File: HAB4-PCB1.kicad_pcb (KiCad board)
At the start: 2 copper layers, 16 parts, among them J1 Barrel_Jack_Switch

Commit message: gnd plane
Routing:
- net Net-(D1-K): track 9.56 -> 44.2 mm, vias 0 -> 1
- net GND: vias 0 -> 12
- added copper zone on B.Cu, net GND
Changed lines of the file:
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@@
 		)
+	)
+	(via
+		(at 23.99 66)
+		(size 0.6)
+		(drill 0.3)
+		(layers "F.Cu" "B.Cu")
+		(net 1)
+	)
+	(via
+		(at 21 19.5)
+		(size 0.6)
+		(drill 0.3)
+		(layers "F.Cu" "B.Cu")
+		(net 1)
+	)
+	(via
+		(at 104 89.54)
+		(size 0.6)
+		(drill 0.3)
+		(layers "F.Cu" "B.Cu")
+		(net 1)
+	)
+	(via
+		(at 59.62 15.92)
+		(size 0.6)
+		(drill 0.3)
+		(layers "F.Cu" "B.Cu")
+		(net 1)
+	)
+	(via
+		(at 44.38 15.92)
+		(size 0.6)
+		(drill 0.3)
+		(layers "F.Cu" "B.Cu")
+		(net 1)
+	)
+	(via
+		(at 23.99 46)
+		(size 0.6)
+		(drill 0.3)
+		(layers "F.Cu" "B.Cu")
+		(net 1)
+	)
+	(via
+		(at 104 43.7)
+		(size 0.6)
+		(drill 0.3)
+		(layers "F.Cu" "B.Cu")
+		(net 1)
+	)
+	(via
+		(at 26.3 92)
+		(size 0.6)
+		(drill 0.3)
+		(layers "F.Cu" "B.Cu")
+		(net 1)
+	)
+	(via
+		(at 79.92 64.27)
+		(size 0.6)
+		(drill 0.3)
+		(layers "F.Cu" "B.Cu")
+		(net 1)
+	)
+	(via
+		(at 90.08 64.27)
+		(size 0.6)
+		(drill 0.3)
+		(layers "F.Cu" "B.Cu")
+		(net 1)
+	)
+	(via
+		(at 23.99 56)
+		(size 0.6)
+		(drill 0.3)
+		(layers "F.Cu" "B.Cu")
+		(net 1)
+	)
+	(via
+		(at 23.99 76)
+		(size 0.6)
+		(drill 0.3)
+		(layers "F.Cu" "B.Cu")
+		(net 1)
 	)
 	(segment
@@
 	)
 	(segment
+		(start 65.38 50.38)
+		(end 55 40)
+		(width 0.2)
+		(layer "F.Cu")
+		(net 8)
+	)
+	(segment
 		(start 38 32.46)
 		(end 44.38 26.08)
@@
 	)
 	(segment
+		(start 67 50.38)
+		(end 65.38 50.38)
+		(width 0.2)
+		(layer "F.Cu")
+		(net 8)
+	)
+	(segment
 		(start 38 33)
 		(end 38 32.46)
@@
 		(net 8)
 	)
+	(via
+		(at 55 40)
+		(size 0.6)
+		(drill 0.3)
+		(layers "F.Cu" "B.Cu")
+		(net 8)
+	)
+	(segment
+		(start 55 36.7)
+		(end 44.38 26.08)
+		(width 0.2)
+		(layer "B.Cu")
+		(net 8)
+	)
+	(segment
+		(start 55 40)
+		(end 55 36.7)
+		(width 0.2)
+		(layer "B.Cu")
+		(net 8)
+	)
 	(segment
 		(start 35.92 46)
@@
 		(net 45)
 	)
+	(zone
+		(net 1)
+		(net_name "GND")
+		(layer "B.Cu")
+		(hatch edge 0.5)
+		(connect_pads
+			(clearance 0.5)
+		)
+		(min_thickness 0.25)
+		(filled_areas_thickness no)
+		(fill yes
+			(thermal_gap 0.5)
+			(thermal_bridge_width 0.5)
+		)
+		(polygon
+			(pts
+				(xy 110 100) (xy 110 12) (xy 12 12) (xy 12 100)
+			)
+		)
+	)
 	(embedded_fonts no)

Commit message: nano GND connect
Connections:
- NANO1 pad 29: unconnected-(NANO1-GND-Pad29) -> GND
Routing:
- net GND: vias 12 -> 13

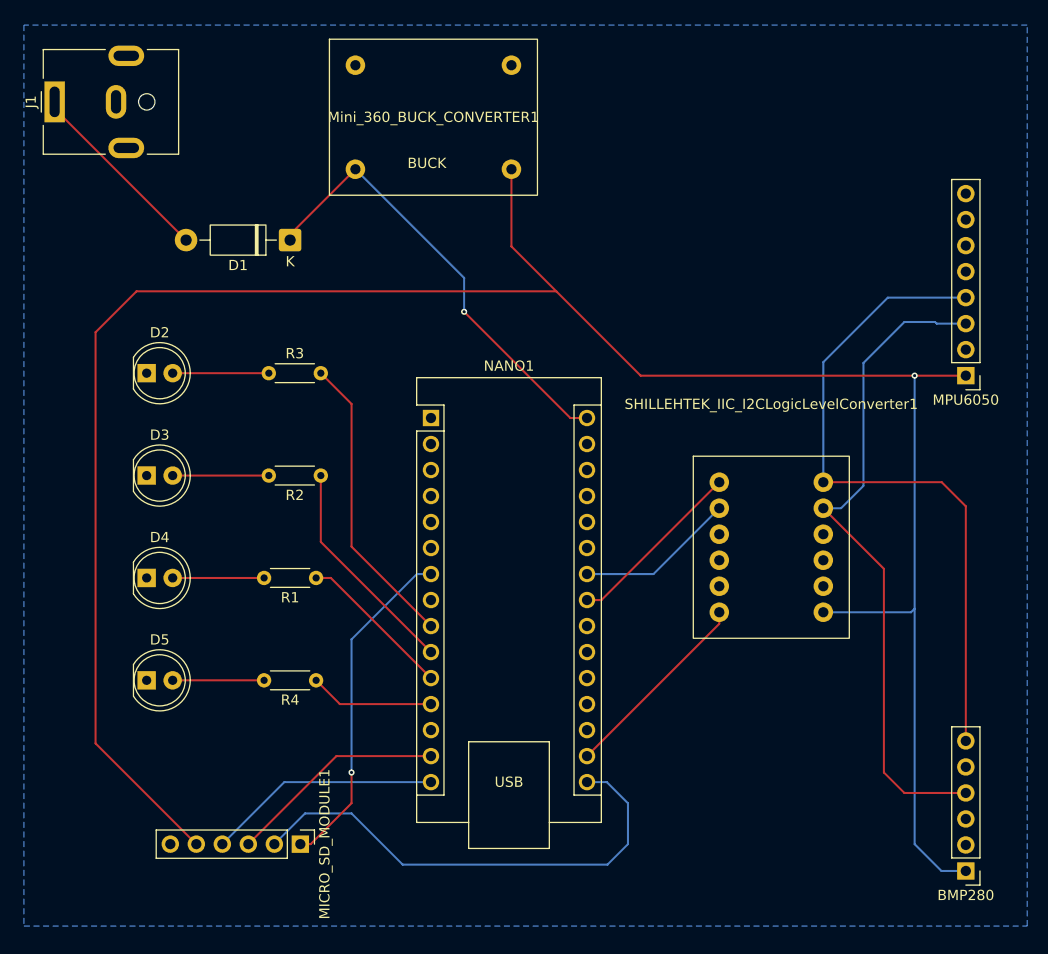
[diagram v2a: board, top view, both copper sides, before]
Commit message: board outline and fix GND pins
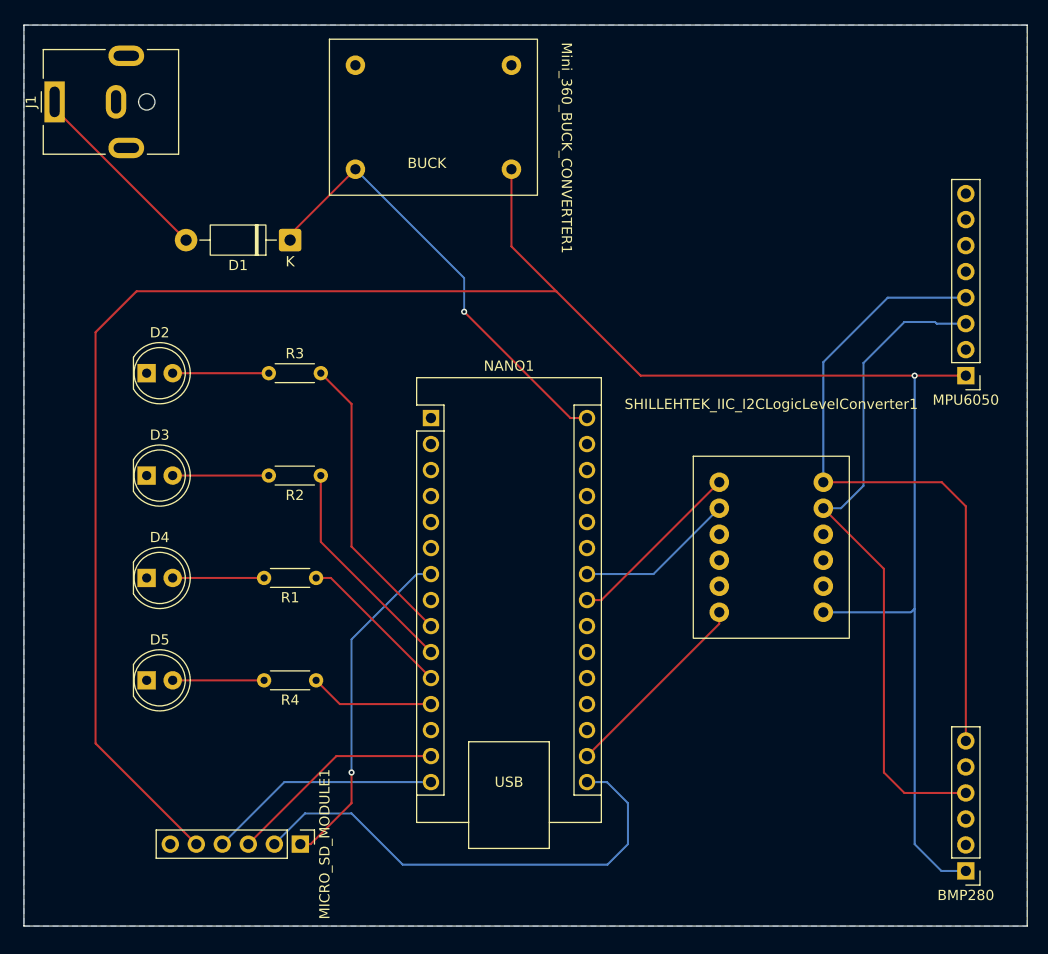
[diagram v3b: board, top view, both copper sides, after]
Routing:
- net GND: vias 13 -> 0
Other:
- board outline added: 98 x 88 mm
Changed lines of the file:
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@@
 		(at 44.38 15.92)
 		(property "Reference" "Mini_360_BUCK_CONVERTER1"
-			(at 7.62 5.08 0)
+			(at 20.62 8.08 270)
 			(unlocked yes)
 			(layer "F.SilkS")
@@
 		)
 	)
-	(via
-		(at 23.99 66)
-		(size 0.6)
-		(drill 0.3)
-		(layers "F.Cu" "B.Cu")
-		(net 1)
-	)
-	(via
-		(at 21 19.5)
-		(size 0.6)
-		(drill 0.3)
-		(layers "F.Cu" "B.Cu")
-		(net 1)
-	)
-	(via
-		(at 104 89.54)
-		(size 0.6)
-		(drill 0.3)
-		(layers "F.Cu" "B.Cu")
-		(net 1)
-	)
-	(via
-		(at 59.62 15.92)
-		(size 0.6)
-		(drill 0.3)
-		(layers "F.Cu" "B.Cu")
-		(net 1)
-	)
-	(via
-		(at 44.38 15.92)
-		(size 0.6)
-		(drill 0.3)
-		(layers "F.Cu" "B.Cu")
-		(net 1)
-	)
-	(via
-		(at 23.99 46)
-		(size 0.6)
-		(drill 0.3)
-		(layers "F.Cu" "B.Cu")
-		(net 1)
-	)
-	(via
-		(at 67 52.92)
-		(size 0.6)
-		(drill 0.3)
-		(layers "F.Cu" "B.Cu")
-		(free yes)
-		(net 1)
-	)
-	(via
-		(at 104 43.7)
-		(size 0.6)
-		(drill 0.3)
-		(layers "F.Cu" "B.Cu")
-		(net 1)
-	)
-	(via
-		(at 26.3 92)
-		(size 0.6)
-		(drill 0.3)
-		(layers "F.Cu" "B.Cu")
-		(net 1)
-	)
-	(via
-		(at 79.92 64.27)
-		(size 0.6)
-		(drill 0.3)
-		(layers "F.Cu" "B.Cu")
-		(net 1)
-	)
-	(via
-		(at 90.08 64.27)
-		(size 0.6)
-		(drill 0.3)
-		(layers "F.Cu" "B.Cu")
-		(net 1)
-	)
-	(via
-		(at 23.99 56)
-		(size 0.6)
-		(drill 0.3)
-		(layers "F.Cu" "B.Cu")
-		(net 1)
-	)
-	(via
-		(at 23.99 76)
-		(size 0.6)
-		(drill 0.3)
-		(layers "F.Cu" "B.Cu")
-		(net 1)
+	(gr_rect
+		(start 12 12)
+		(end 110 100)
+		(stroke
+			(width 0.05)
+			(type default)
+		)
+		(fill no)
+		(layer "Edge.Cuts")
 	)
 	(segment

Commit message: Improve GND and fix Shifter pins
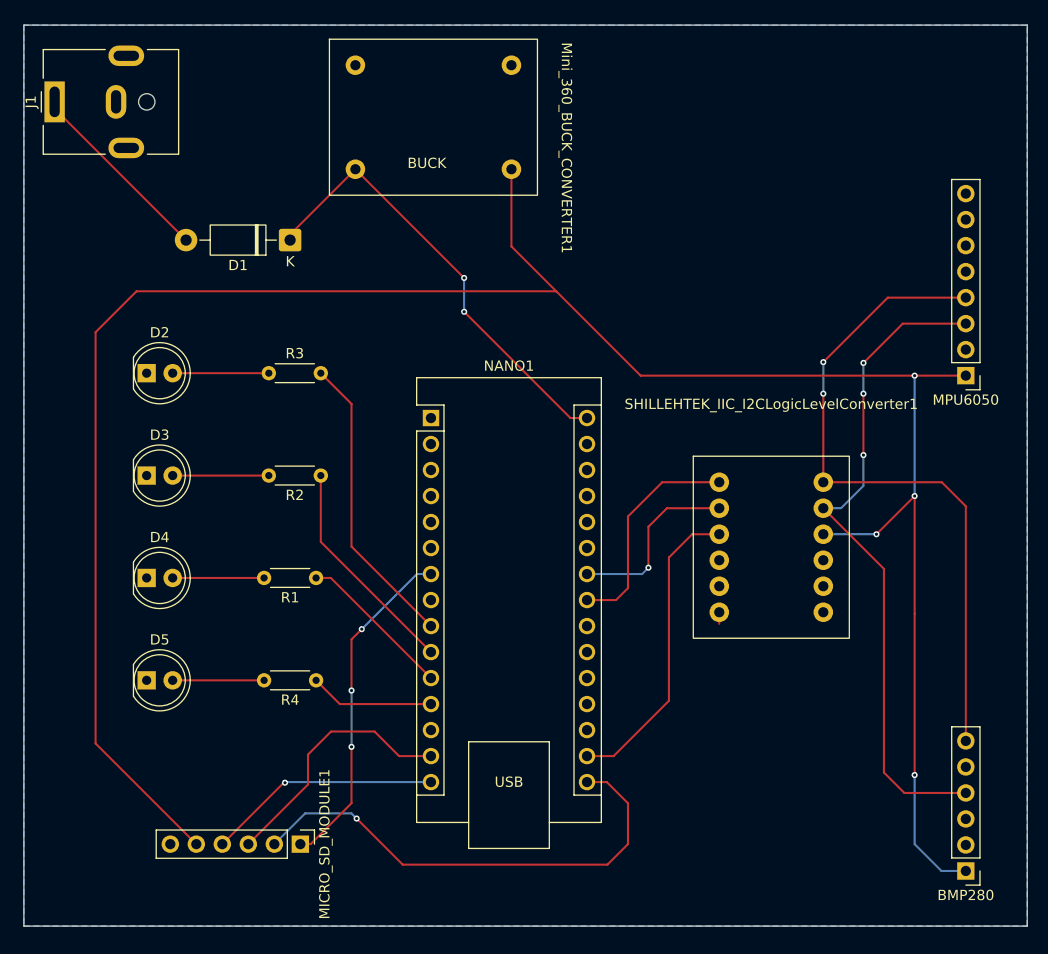
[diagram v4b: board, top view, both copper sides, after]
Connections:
- NANO1 pad 29: GND -> unconnected-(NANO1-GND-Pad29)
- NANO1 pad 8: Net-(NANO1-D5) -> unconnected-(NANO1-D5-Pad8)
- SHILLEHTEK_IIC_I2CLogicLevelConverter1 pad 12: Net-(NANO1-3V3) -> unconnected-(SHILLEHTEK_IIC_I2CLogicLevelConverter1-LV4-Pad12)
- SHILLEHTEK_IIC_I2CLogicLevelConverter1 pad 3: unconnected-(SHILLEHTEK_IIC_I2CLogicLevelConverter1-HV3-Pad3) -> Net-(BMP280-VIN)
- SHILLEHTEK_IIC_I2CLogicLevelConverter1 pad 6: Net-(BMP280-VIN) -> unconnected-(SHILLEHTEK_IIC_I2CLogicLevelConverter1-HV4-Pad6)
- SHILLEHTEK_IIC_I2CLogicLevelConverter1 pad 9: unconnected-(SHILLEHTEK_IIC_I2CLogicLevelConverter1-LV3-Pad9) -> Net-(NANO1-3V3)
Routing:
- net Net-(NANO1-3V3): track 19.4 -> 30.1 mm
- net Net-(NANO1-A4): track 17.7 -> 21.8 mm
- net Net-(MICRO_SD_MODULE1-MOSI): track 21.4 -> 25.1 mm
- net Net-(NANO1-A5): track 15.6 -> 17.9 mm, vias 0 -> 1
- net Net-(BMP280-VIN): track 218.8 -> 220.2 mm, vias 1 -> 4
- net unconnected-(SHILLEHTEK_IIC_I2CLogicLevelConverter1-LV4-Pad12): track 0.00 -> 1.13 mm
- net Net-(BMP280-SCK): track 65.6 -> 65.5 mm, vias 0 -> 3
- net Net-(MICRO_SD_MODULE1-CS): vias 1 -> 3
- net Net-(MICRO_SD_MODULE1-SCK): vias 0 -> 1
- net Net-(MICRO_SD_MODULE1-MISO): vias 0 -> 1
- net Net-(D1-K): vias 1 -> 2
- net Net-(BMP280-SDI): vias 0 -> 2

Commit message: Jumper cables and other
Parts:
- added JP1: Jumper_2_Bridged, My_Footprints2:6mm_jumper, F.Cu at (55.0, 34.0)
- added JP2: Jumper_2_Bridged, My_Footprints2:6mm_jumper, F.Cu at (97.0, 51.0)
- added JP3: Jumper_2_Bridged, My_Footprints2:8mm_jumper, F.Cu at (46.0, 81.0)
- added JP4: Jumper_2_Bridged, My_Footprints2:6mm_jumper, F.Cu at (96.0, 56.0)
- added JP5: Jumper_2_Bridged, My_Footprints2:6mm_jumper, F.Cu at (71.0, 61.0)
- added JP6: Jumper_2_Bridged, My_Footprints2:8mm_jumper, F.Cu at (42.0, 86.0)
- moved R1 2.00 mm to (38.5, 66.0)
- moved R4 2.00 mm to (38.5, 76.0)
- moved R2 1.92 mm to (39.1, 56.0)
- moved J1 1.50 mm to (16.5, 19.5)
- moved R3 1.46 mm to (34.5, 46.0)
- moved MPU6050 1.00 mm to (103.0, 46.2)
- renumbered SHILLEHTEK_IIC_I2CLogicLevelConverter1 to I2C_LVL_SHIFTER1
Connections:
- I2C_LVL_SHIFTER1 pad 1: Net-(BMP280-SDI) -> Net-(I2C_LVL_SHIFTER1-HV1)
- I2C_LVL_SHIFTER1 pad 7: Net-(NANO1-A4) -> Net-(I2C_LVL_SHIFTER1-LV1)
- MICRO_SD_MODULE1 pad 1: Net-(MICRO_SD_MODULE1-CS) -> Net-(JP3-B)
- MICRO_SD_MODULE1 pad 4: Net-(MICRO_SD_MODULE1-MISO) -> Net-(JP6-B)
- MPU6050 pad 3: Net-(BMP280-SCK) -> Net-(JP2-B)
- NANO1 pad 11: Net-(NANO1-D8) -> Net-(JP3-A)
- NANO1 pad 12: Net-(NANO1-D9) -> unconnected-(NANO1-D9-Pad12)
- NANO1 pad 15: Net-(MICRO_SD_MODULE1-MISO) -> Net-(JP6-A)
- NANO1 pad 23: Net-(NANO1-A4) -> Net-(JP5-B)
- NANO1 pad 29: unconnected-(NANO1-GND-Pad29) -> GND
- NANO1 pad 30: Net-(D1-K) -> Net-(JP1-B)
- NANO1 pad 4: unconnected-(NANO1-GND-Pad4) -> GND
- NANO1 pad 7: Net-(MICRO_SD_MODULE1-CS) -> Net-(NANO1-D4)
- NANO1 pad 8: unconnected-(NANO1-D5-Pad8) -> Net-(NANO1-D5)
- R1 pad 1: Net-(NANO1-D8) -> Net-(NANO1-D6)
- R2 pad 1: Net-(NANO1-D7) -> Net-(NANO1-D5)
- R3 pad 2: Net-(NANO1-D6) -> Net-(NANO1-D4)
- R4 pad 1: Net-(NANO1-D9) -> Net-(NANO1-D7)
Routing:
- net Net-(MICRO_SD_MODULE1-CS): track 33.1 -> 0.00 mm, vias 3 -> 0
- net Net-(NANO1-D4): track 0.00 -> 27.9 mm
- net Net-(MICRO_SD_MODULE1-MISO): track 22.9 -> 0.00 mm, vias 1 -> 0
- net Net-(NANO1-A4): track 21.8 -> 0.00 mm
- net Net-(D1-K): track 44.2 -> 23.5 mm, vias 2 -> 0
- net Net-(NANO1-D5): track 0.00 -> 20.7 mm
- net Net-(BMP280-SDI): track 66.1 -> 46.3 mm, vias 2 -> 0
- net Net-(JP1-B): track 0.00 -> 15.5 mm
- net Net-(NANO1-D8): track 15.3 -> 0.00 mm
- net Net-(I2C_LVL_SHIFTER1-LV1): track 0.00 -> 14.4 mm
- net Net-(NANO1-D6): track 29.2 -> 15.2 mm
- net Net-(NANO1-D9): track 12.2 -> 0.00 mm
- net Net-(JP6-A): track 0.00 -> 9.28 mm
- net Net-(JP3-A): track 0.00 -> 9.18 mm
- net Net-(JP3-B): track 0.00 -> 7.83 mm
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
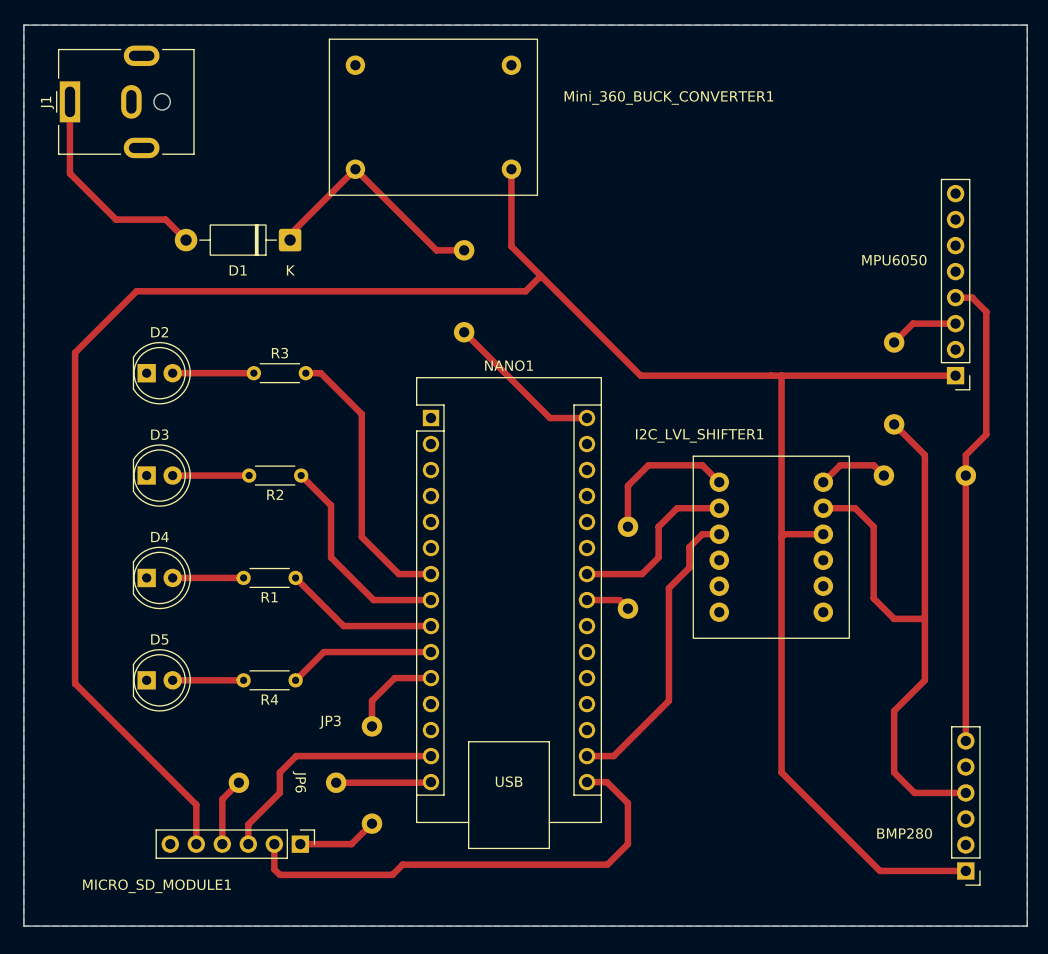
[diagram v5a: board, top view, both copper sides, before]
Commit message: grounding flood plane
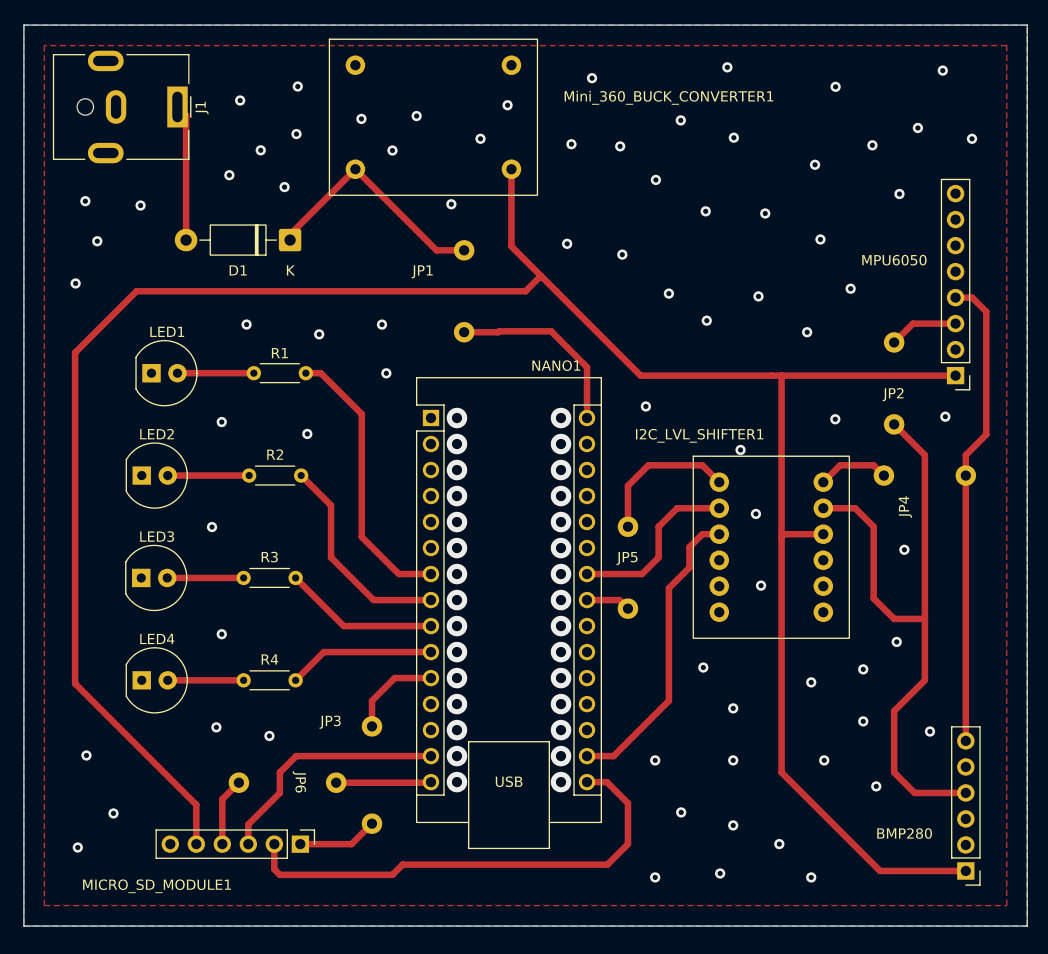
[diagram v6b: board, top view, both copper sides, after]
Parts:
- D2, D3, D4, D5: footprint LED_THT:LED_D5.0mm -> My_Footprints2:JCLPCB_THT_LED_D5.0mm
- R3: renamed from R1; value R -> R3
- moved J1 10.5 mm to (27.0, 20.0), turned to -90 degrees
- moved D2 1.96 mm to (25.9, 46.0)
- moved D3 1.01 mm to (25.0, 56.0)
- moved D5 1.01 mm to (25.0, 76.0)
- moved D4 0.96 mm to (24.9, 66.0)
- renumbered R3 to R1
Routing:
- net +9V: track 21.0 -> 13.3 mm
- net Net-(JP1-B): track 15.5 -> 18.5 mm
- net Net-(D4-A): track 6.93 -> 7.46 mm
- net GND: vias 0 -> 107
- added copper zone on F.Cu, net GND
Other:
- board text added: "JP1"
- board text added: "JP2"
- board text added: "JP4"
- board text added: "JP5"
- board text added: "LED1"
- board text added: "LED2"
- board text added: "LED3"
- board text added: "LED4"

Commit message: final changes
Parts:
- added REF**: CUonOrbit_logo, My_Footprints2:CUonOrbit_logo, F.Cu at (86.2, 21.0)
- renumbered J1 to BARREL_JACK, I2C_LVL_SHIFTER1 to I2C_LVL_SHIFTER, MICRO_SD_MODULE1 to MICRO_SD_MODULE, Mini_360_BUCK_CONVERTER1 to Mini_360_BUCK, NANO1 to NANO
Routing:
- net GND: vias 107 -> 117
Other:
- board text added: "HAB4"
